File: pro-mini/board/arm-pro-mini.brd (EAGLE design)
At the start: 38.1 x 20.3 mm, 55 parts, among them J1 USB, J2 SWD HEADER, Q1 12Mhz, T1 DTA114EET1G (2 X 10K), U1 MCP1754ST-3302E/CB, U2 NUF2042XV6T1G, U3 LPC11U35FHI33/501

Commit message: Updated revision Renamed directory from eagle to board. Added tester board.
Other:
- board text added: "REV 2E OSH"
- board text removed: "REV 2D OSH"
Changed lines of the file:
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@@
 <text x="27.8384" y="17.0434" size="0.762" layer="21" font="vector" ratio="10" rot="SR270">SWD</text>
 <text x="29.21" y="11.1506" size="0.762" layer="21" font="vector" ratio="10">ARM MINI PRO</text>
-<text x="30.099" y="9.9568" size="0.762" layer="21" font="vector" ratio="10">REV 2D OSH</text>
+<text x="30.099" y="9.9568" size="0.762" layer="21" font="vector" ratio="10">REV 2E OSH</text>
 <wire x1="1.27" y1="2.413" x2="1.27" y2="1.27" width="0.1524" layer="21"/>
 <wire x1="11.43" y1="2.413" x2="11.43" y2="1.27" width="0.1524" layer="21"/>

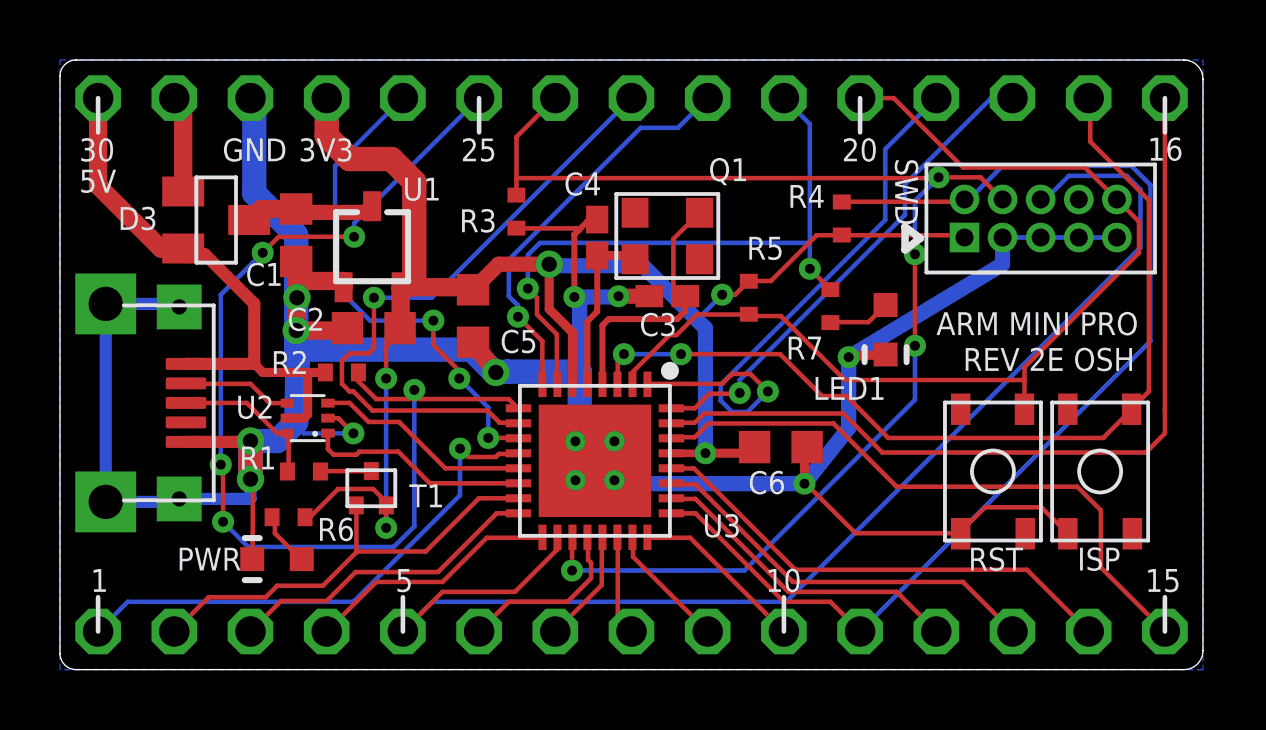
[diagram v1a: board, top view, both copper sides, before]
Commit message: Cleaned up top silkscreen from pads. Bumbed version from 2E to 2F. No stencil change. No semantic change.
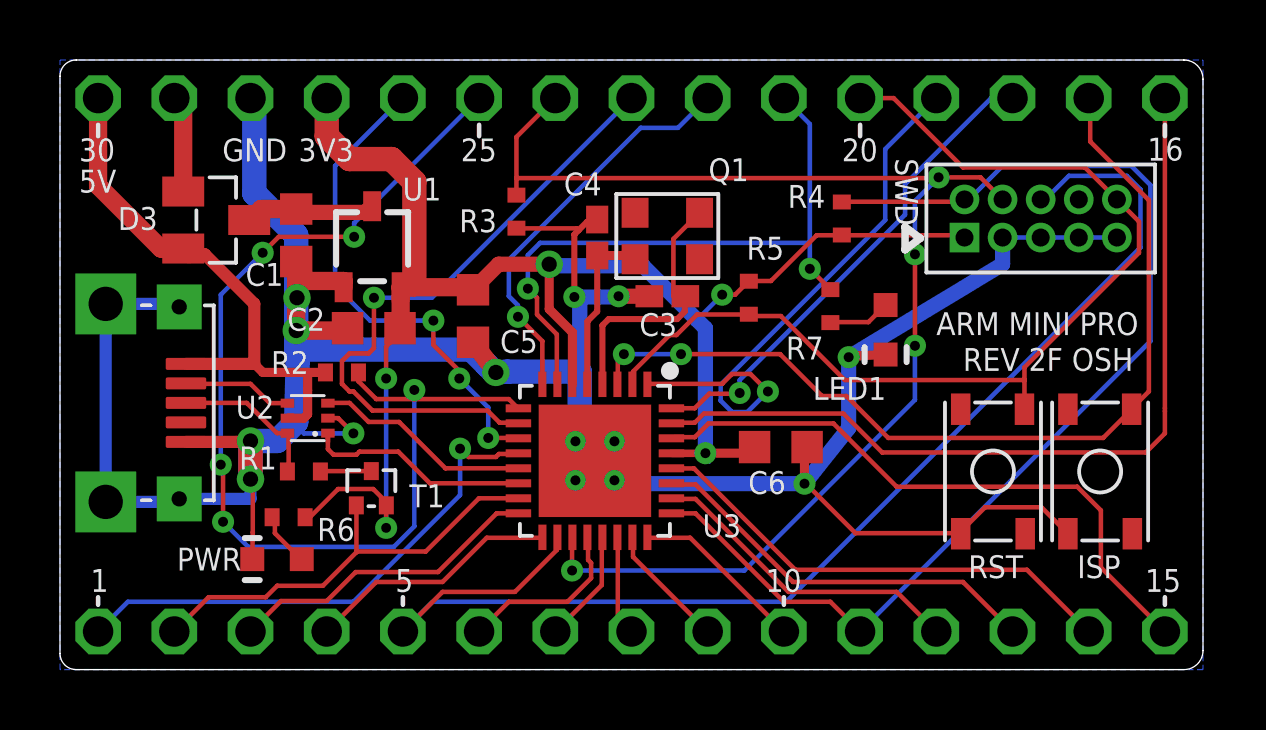
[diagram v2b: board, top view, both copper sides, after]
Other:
- board text added: "REV 2F OSH"
- board text removed: "REV 2E OSH"
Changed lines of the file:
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@@
 <wire x1="0.5388125" y1="0" x2="37.465" y2="0" width="0" layer="20"/>
 <wire x1="37.465" y1="0" x2="38.1" y2="0.635" width="0" layer="20" curve="90"/>
-<text x="30.2768" y="3.302" size="0.762" layer="21" font="vector" ratio="10">RST</text>
-<text x="33.909" y="3.302" size="0.762" layer="21" font="vector" ratio="10">ISP</text>
+<text x="30.2768" y="3.048" size="0.762" layer="21" font="vector" ratio="10">RST</text>
+<text x="33.909" y="3.048" size="0.762" layer="21" font="vector" ratio="10">ISP</text>
 <text x="25.0952" y="8.9916" size="0.762" layer="21" font="vector" ratio="10">LED1</text>
 <text x="3.8960375" y="3.302" size="0.762" layer="21" font="vector" ratio="10">PWR</text>
@@
 <text x="27.8384" y="17.0434" size="0.762" layer="21" font="vector" ratio="10" rot="SR270">SWD</text>
 <text x="29.21" y="11.1506" size="0.762" layer="21" font="vector" ratio="10">ARM MINI PRO</text>
-<text x="30.099" y="9.9568" size="0.762" layer="21" font="vector" ratio="10">REV 2E OSH</text>
-<wire x1="1.27" y1="2.413" x2="1.27" y2="1.27" width="0.1524" layer="21"/>
-<wire x1="11.43" y1="2.413" x2="11.43" y2="1.27" width="0.1524" layer="21"/>
-<wire x1="24.13" y1="2.413" x2="24.13" y2="1.27" width="0.1524" layer="21"/>
-<wire x1="36.83" y1="2.413" x2="36.83" y2="1.27" width="0.1524" layer="21"/>
-<wire x1="26.67" y1="17.907" x2="26.67" y2="19.05" width="0.1524" layer="21"/>
-<wire x1="36.83" y1="17.907" x2="36.83" y2="19.05" width="0.1524" layer="21"/>
-<wire x1="13.97" y1="17.907" x2="13.97" y2="19.05" width="0.1524" layer="21"/>
-<wire x1="1.27" y1="17.907" x2="1.27" y2="19.05" width="0.1524" layer="21"/>
+<text x="30.099" y="9.9568" size="0.762" layer="21" font="vector" ratio="10">REV 2F OSH</text>
+<wire x1="1.27" y1="2.413" x2="1.27" y2="2.159" width="0.1524" layer="21"/>
+<wire x1="11.43" y1="2.413" x2="11.43" y2="2.159" width="0.1524" layer="21"/>
+<wire x1="24.13" y1="2.413" x2="24.13" y2="2.159" width="0.1524" layer="21"/>
+<wire x1="36.83" y1="2.413" x2="36.83" y2="2.159" width="0.1524" layer="21"/>
+<wire x1="26.67" y1="17.78" x2="26.67" y2="18.161" width="0.1524" layer="21"/>
+<wire x1="36.83" y1="17.78" x2="36.83" y2="18.161" width="0.1524" layer="21"/>
+<wire x1="13.97" y1="17.78" x2="13.97" y2="18.161" width="0.1524" layer="21"/>
+<wire x1="1.27" y1="17.78" x2="1.27" y2="18.161" width="0.1524" layer="21"/>
 <text x="5.4102" y="16.9418" size="0.762" layer="21" font="vector" ratio="10">GND</text>
 <text x="7.9502" y="16.9418" size="0.762" layer="21" font="vector" ratio="10">3V3</text>

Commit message: Added diodes/cap circuit for a single button ISP. Grounded two extra pins of the crystal. Swapped the order and increase the spacing between the two buttons. Ready for final auto routing.
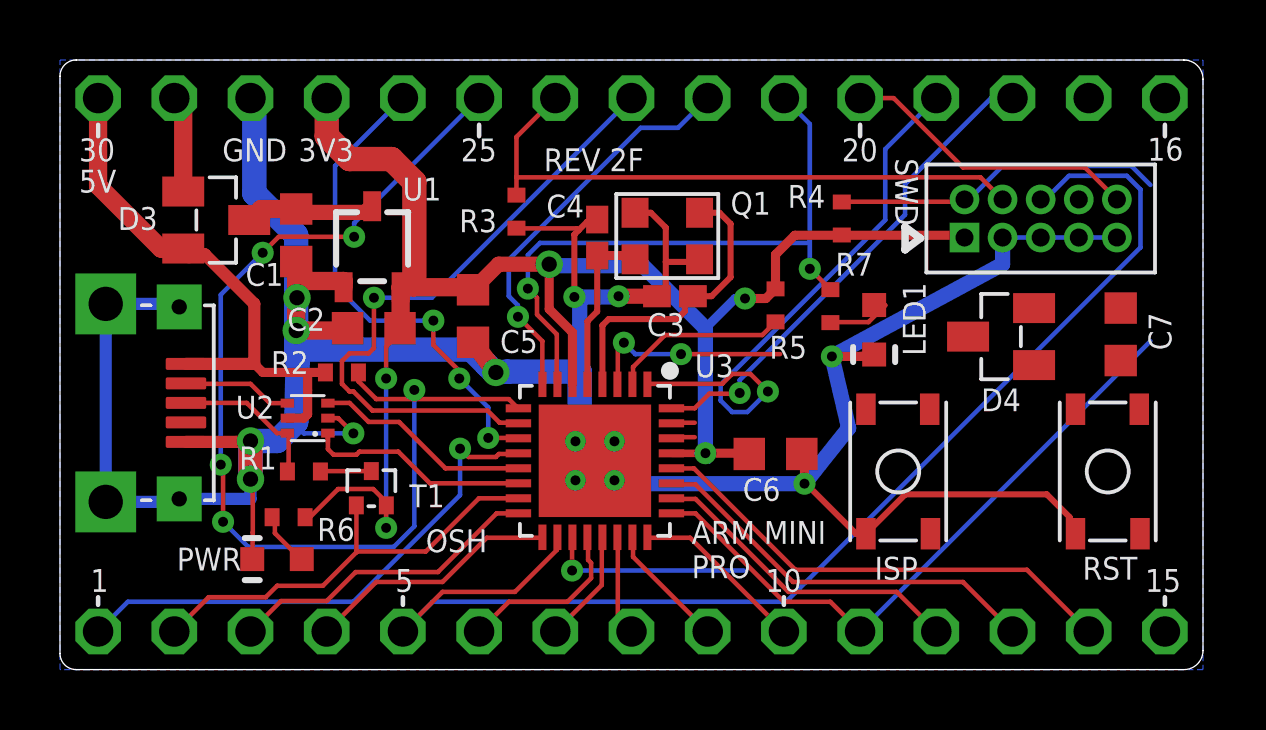
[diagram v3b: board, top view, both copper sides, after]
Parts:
- added C7: 0.1uF, arm-pro-mini:C0603K
- added D4: BAS40-05, arm-pro-mini:SOT23
- moved S1 6.73 mm to (27.9, 6.60)
- moved S2 3.83 mm to (34.9, 6.60)
- moved R5 0.92 mm to (23.9, 12.1)
- moved D1 0.38 mm to (27.1, 11.3)
- moved C6 0.29 mm to (23.9, 7.19)
- moved C3 0.25 mm to (20.5, 12.4)
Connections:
- new net N$8: D4.3, S1.B2
- net +3V3: now also C7.1
- net GND: now also Q1.2, Q1.4
- net PIO0_0-RESET: now also D4.1
- net PIO0_1-ISP_EN: now also C7.2, D4.2; no longer S1.B2
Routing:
- net PIO0_18: track 28.6 -> 0.79 mm
- net PIO0_1-ISP_EN: track 31.2 -> 7.06 mm
- net PIO0_17: track 20.7 -> 0.80 mm
- net PIO0_0-RESET: track 34.0 -> 15.6 mm
- net PIO0_10-SWDCLK: track 42.9 -> 27.1 mm, vias 4 -> 1
- net GND: track 112.8 -> 119.6 mm
- net PIO0_15-SWDIO: track 37.9 -> 32.7 mm
- net N$1: track 9.55 -> 10.5 mm
- net +3V3: track 55.2 -> 56.0 mm
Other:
- board text added: "OSH"
- board text added: "REV 2F"
- board text removed: "REV 2F OSH"

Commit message: Performed final auto routing.
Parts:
- moved D4 0.08 mm to (31.4, 11.2)
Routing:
- net PIO0_1-ISP_EN: track 7.06 -> 37.3 mm, vias 2 -> 4
- net PIO0_18: track 0.79 -> 29.4 mm, vias 0 -> 1
- net PIO0_0-RESET: track 15.6 -> 40.7 mm, vias 0 -> 2
- net PIO0_17: track 0.80 -> 20.2 mm
- net PIO0_10-SWDCLK: track 27.1 -> 42.8 mm, vias 1 -> 4
- net +3V3: track 56.0 -> 62.6 mm
- net PIO0_15-SWDIO: track 32.7 -> 37.9 mm
- net N$8: track 0.00 -> 3.03 mm
- net N$6: track 2.45 -> 1.73 mm
- net GND: track 119.6 -> 120.2 mm
